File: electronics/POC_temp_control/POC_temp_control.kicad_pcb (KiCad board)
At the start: 2 copper layers, 109.2 x 78.7 mm, 210 parts, among them J1 Conn_01x02, J2 Conn_01x07, J3 Conn_01x05, J4 Conn_01x06, J5 Conn_01x04, J6 Conn_01x06, Q1 PXT8050, Q10 BC847A, Q11 BC858B, Q12 BC847A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

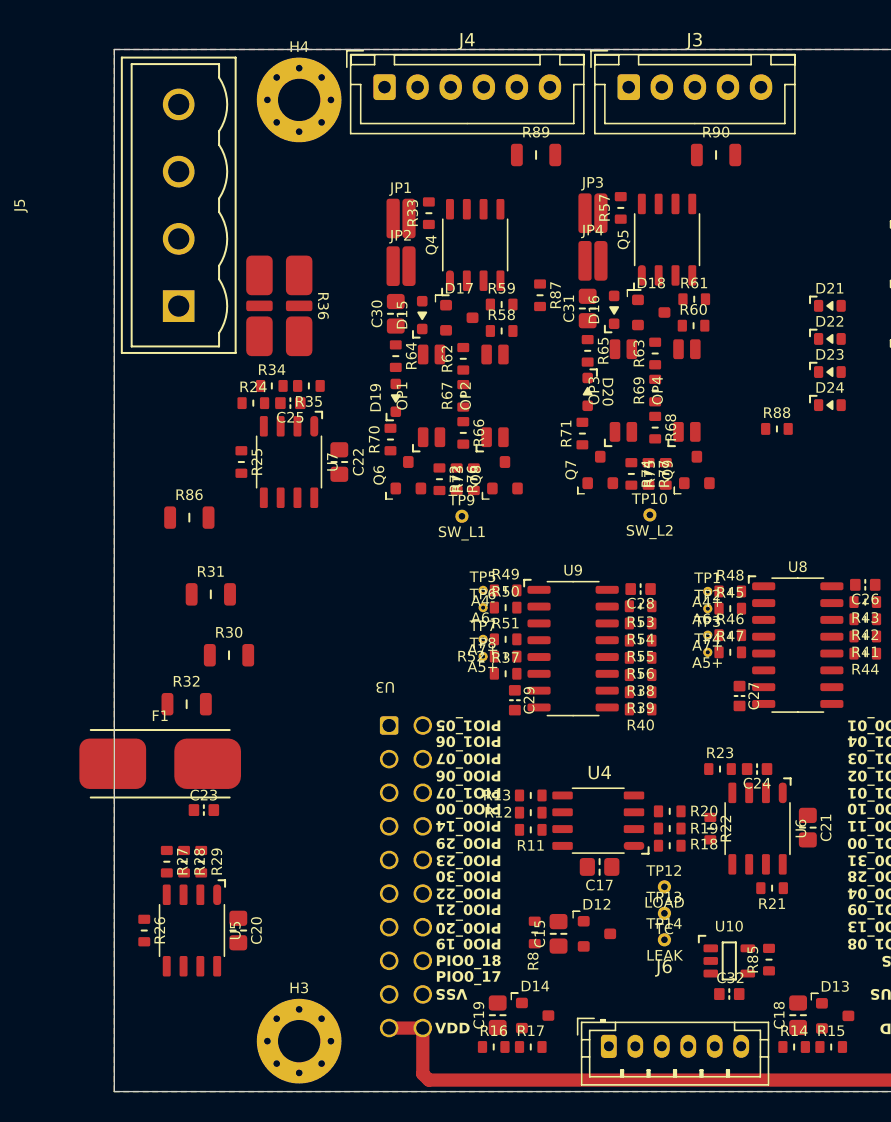
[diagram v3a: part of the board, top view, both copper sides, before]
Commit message: some placing and routing done
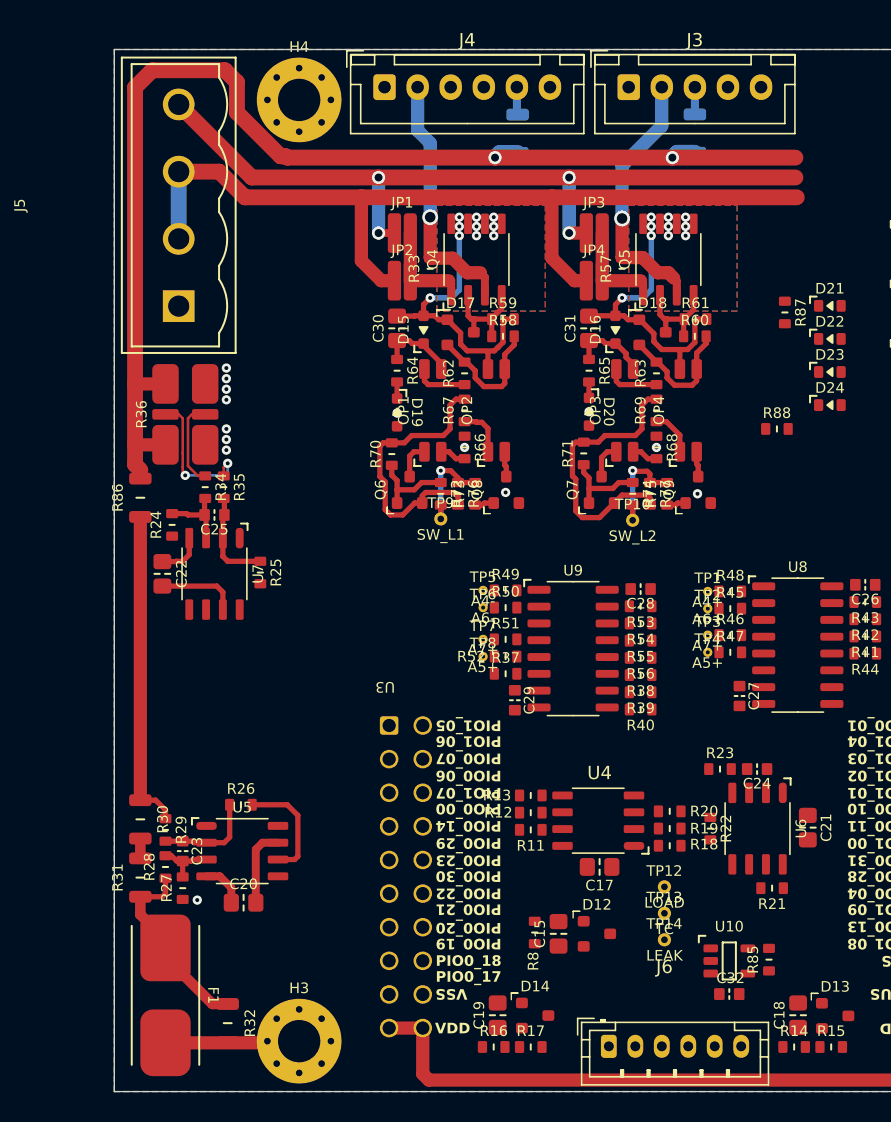
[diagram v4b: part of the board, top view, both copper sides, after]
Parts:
- R89, R90: moved to B.Cu
- moved R32 24.3 mm to (32.7, 97.7), turned to -90 degrees
- moved R31 22.1 mm to (26.1, 86.7), turned to 90 degrees
- moved R87 18.5 mm to (74.8, 44.0)
- moved F1 17.5 mm to (28.0, 95.6), turned to -90 degrees
- moved C22 15.8 mm to (27.8, 63.8)
- moved R30 14.1 mm to (26.1, 82.3), turned to -90 degrees
- moved R26 12.0 mm to (33.7, 81.2), turned to 0 degrees
- moved R24 11.1 mm to (28.5, 60.0), turned to 90 degrees
- moved R36 10.8 mm to (29.5, 51.7), turned to 90 degrees
- moved C25 10.2 mm to (31.7, 59.3)
- moved U7 10.2 mm to (31.7, 63.8)
- moved R35 10.00 mm to (32.4, 57.2), turned to -90 degrees
- moved R34 9.16 mm to (31.0, 57.2), turned to -90 degrees
- moved R25 8.47 mm to (35.2, 63.6)
- moved U5 7.10 mm to (33.8, 84.7), turned to 0 degrees
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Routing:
- net /LOAD: track 0.00 -> 92.5 mm, vias 0 -> 2
- net /AC1: track 0.00 -> 68.4 mm
- net /AC2: track 0.00 -> 59.8 mm, vias 0 -> 4
- net /VD3.3V+: track 49.5 -> 91.9 mm
- net /LEAK-DIFF: track 0.00 -> 24.3 mm
- net /SW_S2: track 0.00 -> 21.7 mm, vias 0 -> 10
- net /SW_S1: track 0.00 -> 21.7 mm, vias 0 -> 10
- net /COM2: track 0.00 -> 20.1 mm, vias 0 -> 1
- net /COM1: track 0.00 -> 19.4 mm, vias 0 -> 1
- net /LEAK+DIFF: track 0.00 -> 14.7 mm
- net /VA8V+: track 24.0 -> 36.0 mm
- net /LOAD_SEN: track 0.00 -> 10.9 mm, vias 0 -> 2
- net Net-(D17-K2): track 0.00 -> 9.91 mm
- net Net-(D18-K2): track 0.00 -> 9.67 mm
- net /LEAK_DIFF: track 0.00 -> 8.48 mm
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- added copper zone on B.Cu, net /SW_S1
- added copper zone on F.Cu, net /SW_S1
- added copper zone on B.Cu, net /SW_S2
- added copper zone on F.Cu, net /SW_S2

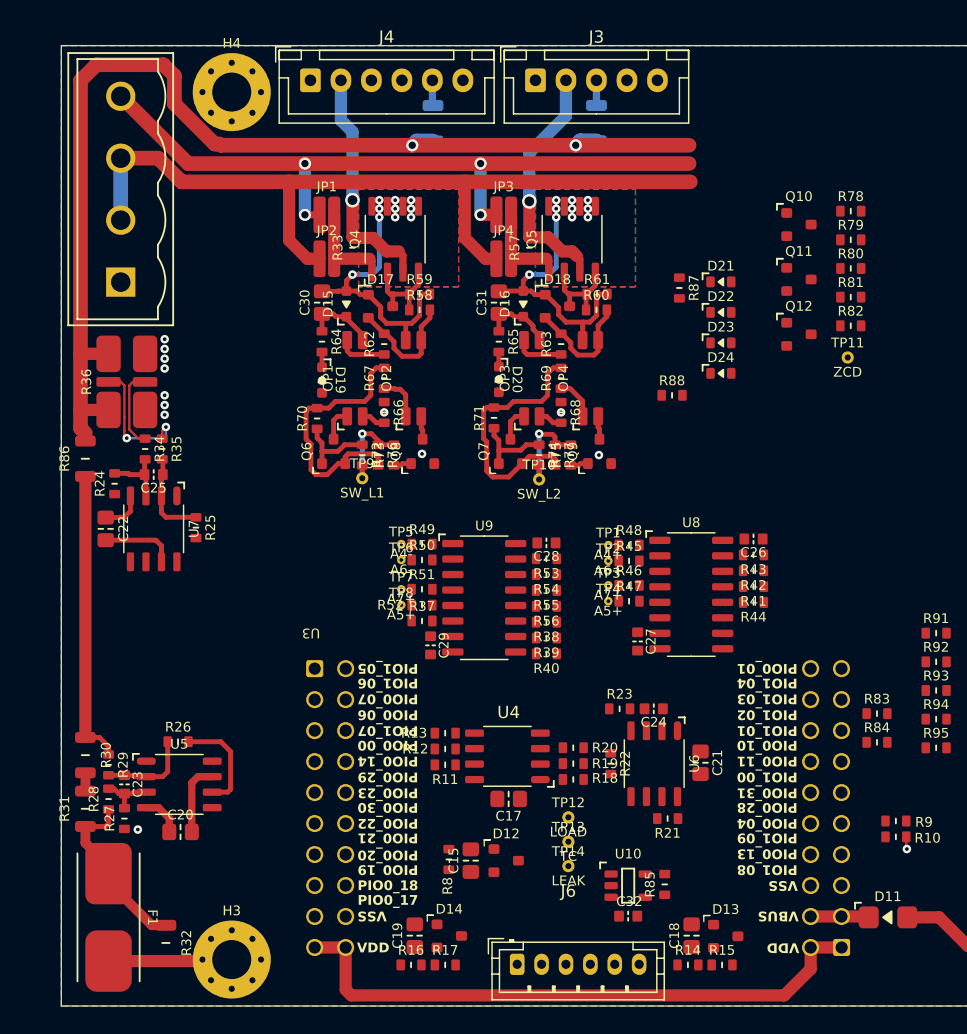
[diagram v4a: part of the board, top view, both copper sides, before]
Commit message: further work on place and route, fixed some things with schematic
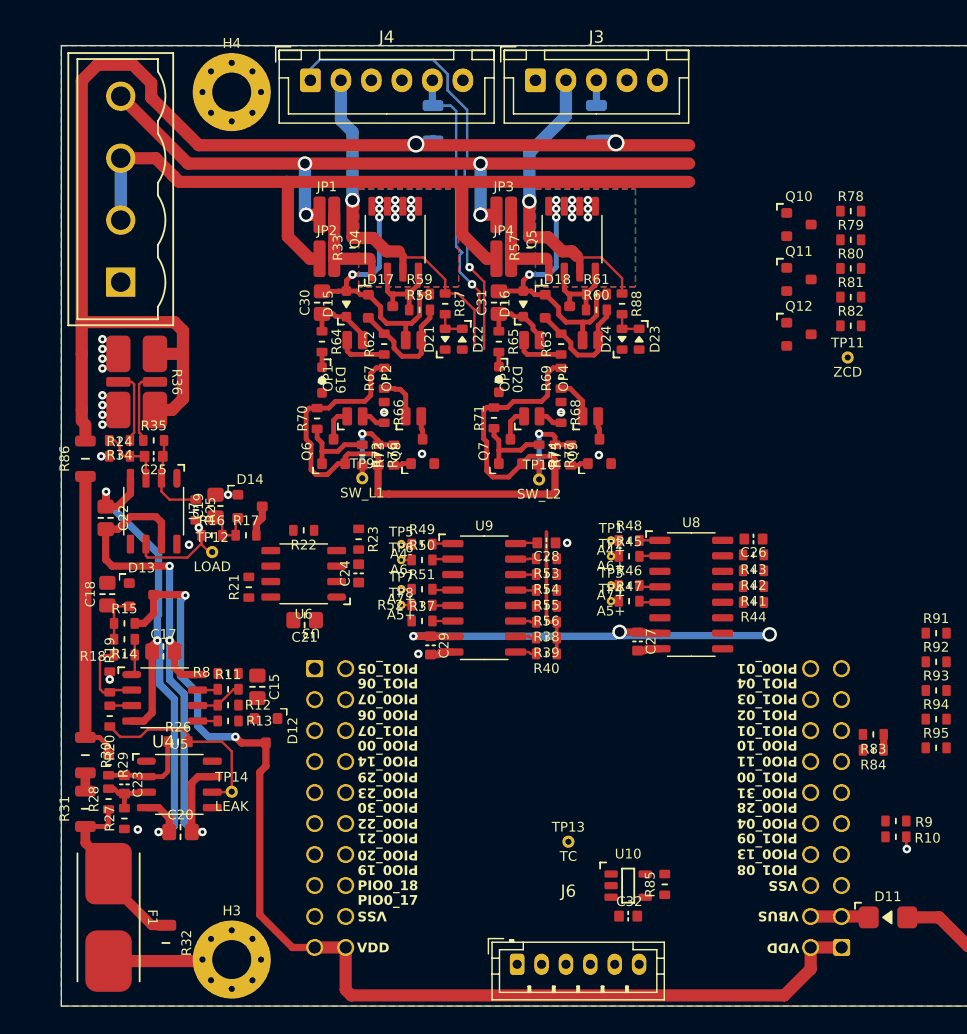
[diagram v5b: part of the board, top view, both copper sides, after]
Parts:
- moved R15 56.4 mm to (29.3, 71.5)
- moved C18 55.5 mm to (27.9, 69.1)
- moved D13 55.5 mm to (30.7, 69.2)
- moved R14 53.4 mm to (29.3, 72.8), turned to 180 degrees
- moved R21 39.2 mm to (39.5, 68.5), turned to 90 degrees
- moved D14 38.8 mm to (39.6, 61.9)
- moved C19 38.8 mm to (36.8, 61.9)
- moved R16 38.8 mm to (36.5, 64.3)
- moved R17 38.8 mm to (39.3, 64.3)
- moved R19 38.6 mm to (28.1, 76.3), turned to 90 degrees
- moved R18 38.2 mm to (29.3, 74.1), turned to 180 degrees
- moved R20 38.1 mm to (28.1, 79.1), turned to -90 degrees
- moved TP12 36.4 mm to (36.5, 65.7)
- moved C21 34.5 mm to (44.1, 71.2), turned to 180 degrees
- moved U6 32.7 mm to (44.0, 67.4), turned to 180 degrees
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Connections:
- R41 pad 1: /TC1 -> /COM1
- R42 pad 1: /COM1 -> /TC1
- R43 pad 1: /TC2 -> /COM2
- R44 pad 1: /COM2 -> /TC2
- U3 pad 23: unconnected-(U3B-PIO0_06-Pad23) -> /LEAK_FILT
- U3 pad 28: unconnected-(U3B-PIO0_14-Pad28) -> /LOAD_FILT
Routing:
- net /VA4.5V-: track 20.7 -> 98.5 mm, vias 0 -> 6
- net /VD3.3V+: track 91.9 -> 169.3 mm, vias 0 -> 2
- net /VA8V+: track 36.0 -> 73.6 mm, vias 0 -> 3
- net /TC1: track 0.00 -> 36.9 mm, vias 0 -> 1
- net /LOAD2: track 2.10 -> 21.6 mm, vias 0 -> 1
- net /LOAD: track 92.5 -> 105.4 mm
- net /COM1: track 19.4 -> 30.9 mm
- net /LOAD_DIFF: track 0.00 -> 10.0 mm, vias 0 -> 1
- net /LEAK_DIFF: track 8.48 -> 16.6 mm
- net Net-(U4--IN1): track 0.00 -> 6.61 mm
- net /COM2: track 20.1 -> 25.5 mm
- net /LOAD_SEN: track 10.9 -> 6.04 mm, vias 2 -> 0
- net /LEAK_FILT: track 0.00 -> 4.83 mm
- net /LOAD_FILT: track 0.00 -> 4.30 mm
- net Net-(U4--IN2): track 0.00 -> 3.90 mm
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
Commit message: WIP further routing
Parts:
- removed R91, R92, R94, R95: 10K, SquantorResistor:R_0603_hand
- moved R81 54.3 mm to (35.0, 37.7), turned to 90 degrees
- moved R82 54.3 mm to (35.0, 40.5), turned to 90 degrees
- moved R78 49.2 mm to (40.0, 43.9), turned to -90 degrees
- moved R79 48.9 mm to (40.0, 41.1), turned to -90 degrees
- moved R80 47.8 mm to (41.3, 47.1)
- moved Q12 47.7 mm to (37.5, 40.5)
- moved Q10 47.4 mm to (37.5, 43.9)
- moved TP11 45.3 mm to (43.4, 47.0)
- moved Q11 42.1 mm to (42.5, 43.6)
- moved TP13 34.2 mm to (39.7, 67.2)
- moved R93 9.85 mm to (90.7, 85.4), turned to 180 degrees
- moved R40 0.90 mm to (63.9, 74.9)
- moved R23 0.87 mm to (48.8, 65.4)
- moved R22 0.87 mm to (44.3, 64.7)
- moved C24 0.87 mm to (48.8, 68.2)
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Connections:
- J2 pad 2: /+5VD -> /VD5V+
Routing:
- net /VA4.5V-: track 98.5 -> 216.5 mm
- net /VA8V+: track 73.6 -> 184.1 mm, vias 3 -> 5
- net /TC2: track 0.00 -> 83.7 mm, vias 0 -> 5
- net /VA3.3V+: track 29.6 -> 103.4 mm, vias 0 -> 1
- net /VD3.3V+: track 169.3 -> 225.2 mm, vias 2 -> 12
- net /TC1: track 36.9 -> 90.5 mm, vias 1 -> 5
- net /COM1: track 30.9 -> 79.9 mm, vias 1 -> 3
- net /LOAD1: track 2.06 -> 50.8 mm, vias 0 -> 3
- net /COM2: track 25.5 -> 64.5 mm, vias 1 -> 3
- net /LOAD2: track 21.6 -> 57.1 mm, vias 1 -> 3
- net /MUX_S0: track 1.72 -> 36.7 mm, vias 0 -> 1
- net /TC+DIFF: track 0.00 -> 34.0 mm, vias 0 -> 2
- net /MUX_EN: track 1.68 -> 35.3 mm
- net /LOAD_FILT: track 4.30 -> 36.8 mm, vias 0 -> 2
- net /MUX_S2: track 1.74 -> 33.4 mm, vias 0 -> 1
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- added copper zone on F.Cu, net /VD5V+
- removed copper zone on F.Cu, net /+5VD

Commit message: WIP silk placement
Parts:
- D10: value GRN -> Power On
- H1, H2, H3, H4: value MountingHole -> M3
- TP7: value A7+ -> A7-
- TP8: value A5+ -> A5-
- moved R83 16.1 mm to (77.8, 90.3)
- moved R84 16.1 mm to (77.8, 91.6)
- moved R93 16.1 mm to (77.8, 95.1)
- moved R9 5.09 mm to (93.5, 92.7), turned to -90 degrees
- moved R10 3.72 mm to (92.2, 92.7), turned to 90 degrees
- moved C32 1.00 mm to (71.6, 95.5)
- moved TP12 0.18 mm to (36.4, 65.5)
- moved R22 0.10 mm to (44.3, 64.6)
- moved D12 0.10 mm to (41.0, 80.3)
- moved U6 0.06 mm to (44.3, 68.2)
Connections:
- R9 pad 2: /+5VD -> /VD5V+
- U3 pad 21: unconnected-(U3B-PIO1_06-Pad21) -> /SW_LOAD_1
- U3 pad 22: unconnected-(U3B-PIO1_05-Pad22) -> /SW_LOAD_2
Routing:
- net /ZCD: track 4.73 -> 66.3 mm, vias 0 -> 2
- net /VD5V+: track 24.4 -> 67.0 mm
- net /VD3.3V+: track 225.2 -> 256.3 mm, vias 12 -> 14
- net /SW_LOAD_2: track 8.25 -> 38.1 mm
- net /I2C_SDA: track 12.0 -> 36.8 mm, vias 0 -> 2
- net /I2C_SCL: track 15.7 -> 39.7 mm, vias 0 -> 3
- net /!UI_INT: track 12.8 -> 31.0 mm
- net /SW_LOAD_1: track 7.88 -> 25.1 mm
- net /POWER_SENSE: track 0.00 -> 9.57 mm
- net /GND: track 22.1 -> 31.0 mm, vias 57 -> 60
- net Net-(U10-WP): track 0.00 -> 1.60 mm
- net /LOAD_FILT: track 36.8 -> 35.8 mm
- net /LOAD_DIFF: track 10.0 -> 9.40 mm

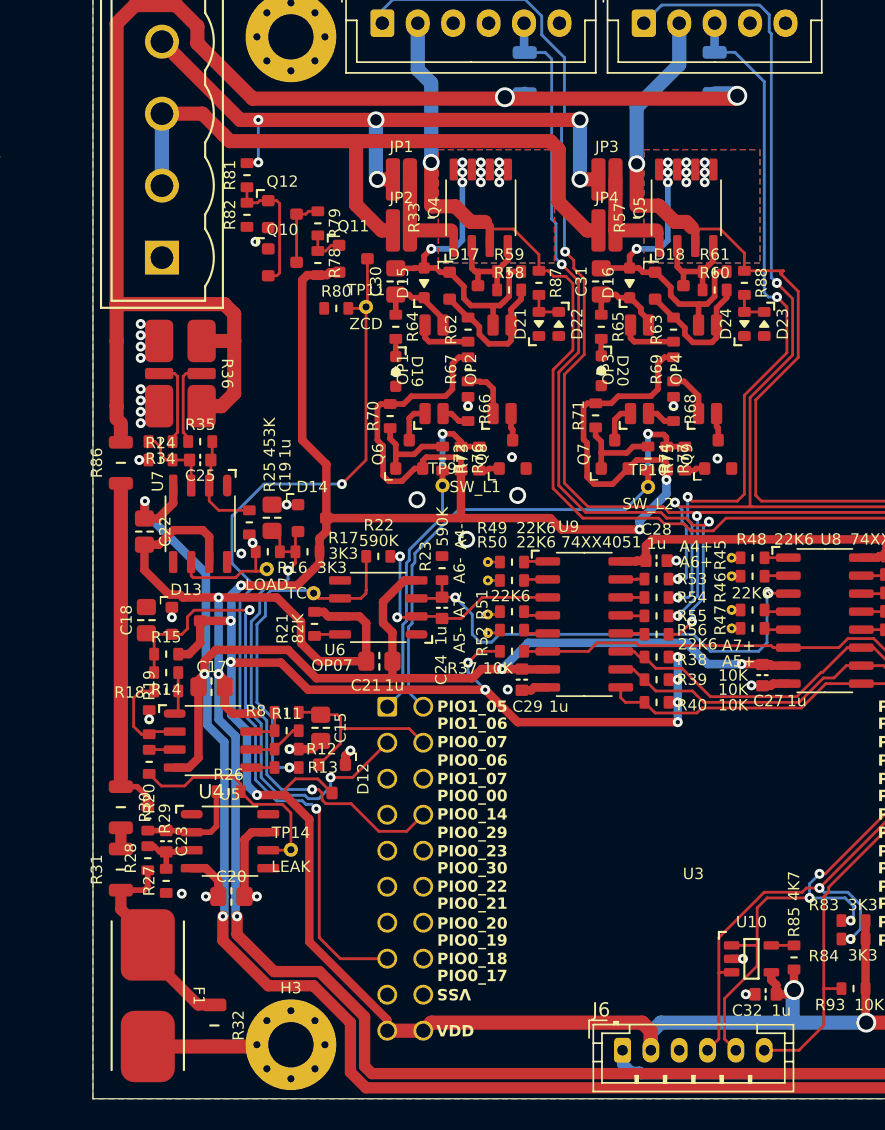
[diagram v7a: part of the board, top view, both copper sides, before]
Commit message: updated silk placements and component values
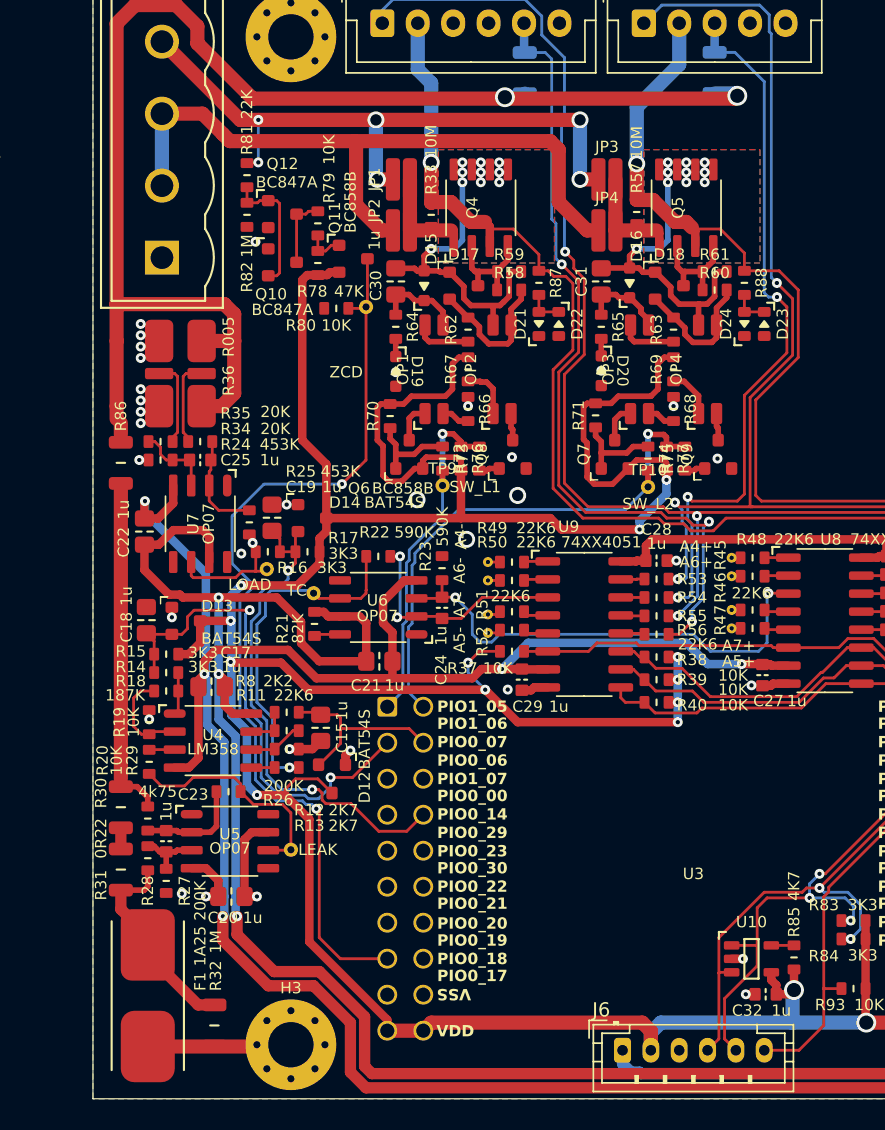
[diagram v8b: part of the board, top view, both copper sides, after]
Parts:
- D12, D13, D14: value ~ -> BAT54S
- moved R57 0.40 mm to (62.5, 40.3)
- moved D15 0.20 mm to (47.5, 45.5)
- moved R33 0.20 mm to (48.0, 40.5)
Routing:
- net /COM2: track 64.5 -> 64.0 mm
